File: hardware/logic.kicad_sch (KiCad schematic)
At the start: 19 parts, among them IC1 UCC2946DG4, IC2 SN74LVC1G74DCTR, IC3 SN74LVC1G74DCTR, Q1 BSS123, U1 74157, U2 4011, U3 4081, U4 4071

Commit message: kończymy balet na dziś
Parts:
- C1, C2, C3, C4: footprint Capacitor_SMD:C_0201_0603Metric_Pad0.64x0.40mm_HandSolder -> Capacitor_SMD:C_0603_1608Metric_Pad1.08x0.95mm_HandSolder
- R3, R6, R7, R8, R9: footprint Resistor_SMD:R_0603_1608Metric -> Resistor_SMD:R_0603_1608Metric_Pad0.98x0.95mm_HandSolder
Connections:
- net AS_COMMADNS+WD_OK renamed AS_COMMADNS_OK
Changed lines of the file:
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@@
     (effects (font (size 1.27 1.27)) (justify left bottom))
   )
-  (label "AS_COMMADNS+WD_OK" (at 219.71 77.47 0)
+  (label "AS_COMMADNS_OK" (at 219.71 77.47 0)
     (effects (font (size 1.27 1.27)) (justify left bottom))
   )
@@
     (property "Reference" "C4" (id 0) (at 80.01 86.36 90))
     (property "Value" "100nF" (id 1) (at 82.55 85.09 90))
-    (property "Footprint" "Capacitor_SMD:C_0201_0603Metric_Pad0.64x0.40mm_HandSolder" (id 2) (at 86.36 82.55 0)
+    (property "Footprint" "Capacitor_SMD:C_0603_1608Metric_Pad1.08x0.95mm_HandSolder" (id 2) (at 86.36 82.55 0)
       (effects (font (size 1.27 1.27)) hide)
     )
@@
       (effects (font (size 1.27 1.27)) (justify left))
     )
-    (property "Footprint" "Resistor_SMD:R_0603_1608Metric" (id 2) (at 41.91 133.35 0)
+    (property "Footprint" "Resistor_SMD:R_0603_1608Metric_Pad0.98x0.95mm_HandSolder" (id 2) (at 41.91 133.35 0)
       (effects (font (size 1.27 1.27)) hide)
     )
@@
       (effects (font (size 1.27 1.27)) (justify left))
     )
-    (property "Footprint" "Resistor_SMD:R_0603_1608Metric" (id 2) (at 63.5 120.65 0)
+    (property "Footprint" "Resistor_SMD:R_0603_1608Metric_Pad0.98x0.95mm_HandSolder" (id 2) (at 63.5 120.65 0)
       (effects (font (size 1.27 1.27)) hide)
     )
@@
       (effects (font (size 1.27 1.27)) (justify left))
     )
-    (property "Footprint" "Capacitor_SMD:C_0201_0603Metric_Pad0.64x0.40mm_HandSolder" (id 2) (at 72.39 129.54 0)
+    (property "Footprint" "Capacitor_SMD:C_0603_1608Metric_Pad1.08x0.95mm_HandSolder" (id 2) (at 72.39 129.54 0)
       (effects (font (size 1.27 1.27)) hide)
     )
@@
       (effects (font (size 1.27 1.27)) (justify left))
     )
-    (property "Footprint" "Resistor_SMD:R_0603_1608Metric" (id 2) (at 63.5 107.95 0)
+    (property "Footprint" "Resistor_SMD:R_0603_1608Metric_Pad0.98x0.95mm_HandSolder" (id 2) (at 63.5 107.95 0)
       (effects (font (size 1.27 1.27)) hide)
     )
@@
       (effects (font (size 1.27 1.27)) (justify left))
     )
-    (property "Footprint" "Resistor_SMD:R_0603_1608Metric" (id 2) (at 58.42 85.09 0)
+    (property "Footprint" "Resistor_SMD:R_0603_1608Metric_Pad0.98x0.95mm_HandSolder" (id 2) (at 58.42 85.09 0)
       (effects (font (size 1.27 1.27)) hide)
     )
@@
       (effects (font (size 1.27 1.27)) (justify left))
     )
-    (property "Footprint" "Resistor_SMD:R_0603_1608Metric" (id 2) (at 52.07 85.09 0)
+    (property "Footprint" "Resistor_SMD:R_0603_1608Metric_Pad0.98x0.95mm_HandSolder" (id 2) (at 52.07 85.09 0)
       (effects (font (size 1.27 1.27)) hide)
     )
@@
       (effects (font (size 1.27 1.27)) (justify left))
     )
-    (property "Footprint" "Capacitor_SMD:C_0201_0603Metric_Pad0.64x0.40mm_HandSolder" (id 2) (at 88.9 130.81 0)
+    (property "Footprint" "Capacitor_SMD:C_0603_1608Metric_Pad1.08x0.95mm_HandSolder" (id 2) (at 88.9 130.81 0)
       (effects (font (size 1.27 1.27)) hide)
     )
@@
       (effects (font (size 1.27 1.27)) (justify left))
     )
-    (property "Footprint" "Capacitor_SMD:C_0201_0603Metric_Pad0.64x0.40mm_HandSolder" (id 2) (at 82.55 109.22 0)
-      (effects (font (size 1.27 1.27)) hide)
-    )
+    (property "Footprint" "Capacitor_SMD:C_0603_1608Metric_Pad1.08x0.95mm_HandSolder" (id 2) (at 82.55 109.22 0)
+      (effects (font (size 1.27 1.27)) hide)
+    )

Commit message: kurde no jeszcze nie skonczylem ale sune dalej
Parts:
- C32, C33: footprint Capacitor_SMD:C_0201_0603Metric_Pad0.64x0.40mm_HandSolder -> Capacitor_SMD:C_0603_1608Metric_Pad1.08x0.95mm_HandSolder
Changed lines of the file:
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@@
       (effects (font (size 1.27 1.27)) (justify left))
     )
-    (property "Footprint" "Capacitor_SMD:C_0201_0603Metric_Pad0.64x0.40mm_HandSolder" (id 2) (at 205.74 31.75 0)
+    (property "Footprint" "Capacitor_SMD:C_0603_1608Metric_Pad1.08x0.95mm_HandSolder" (id 2) (at 205.74 31.75 0)
       (effects (font (size 1.27 1.27)) hide)
     )
@@
       (effects (font (size 1.27 1.27)) (justify left))
     )
-    (property "Footprint" "Capacitor_SMD:C_0201_0603Metric_Pad0.64x0.40mm_HandSolder" (id 2) (at 237.49 38.1 0)
+    (property "Footprint" "Capacitor_SMD:C_0603_1608Metric_Pad1.08x0.95mm_HandSolder" (id 2) (at 237.49 38.1 0)
       (effects (font (size 1.27 1.27)) hide)
     )

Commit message: fixed references addet tp;s mam pojutrze przejebany egzamin nara
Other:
- note added: "AND2"
- note added: "NAND1"
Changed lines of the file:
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@@
     (effects (font (size 1.27 1.27) italic) (justify left bottom))
+  )
+  (text "AND2" (at 149.86 146.05 0)
+    (effects (font (size 1.27 1.27)) (justify left bottom))
+  )
+  (text "NAND1" (at 147.32 71.12 0)
+    (effects (font (size 1.27 1.27)) (justify left bottom))
   )
   (text "WD operation:\nPage 7 of Datasheet" (at 99.06 102.87 0)

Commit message: L4 port
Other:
- note added: "07072023 zwora do ominięcia przycisków"

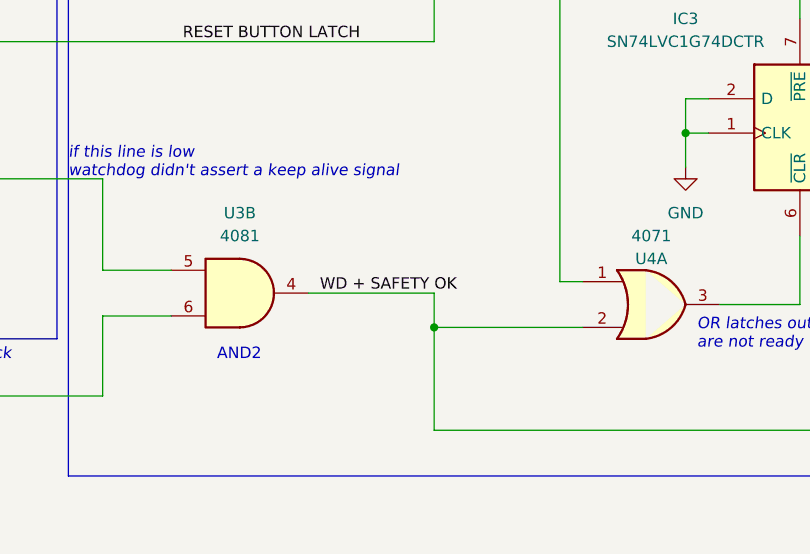
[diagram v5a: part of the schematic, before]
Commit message: first working state, valves forced activation
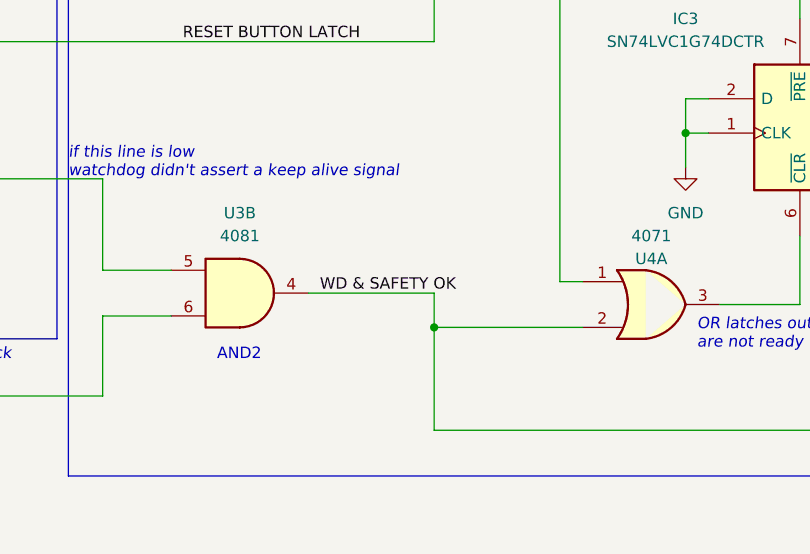
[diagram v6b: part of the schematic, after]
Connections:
- net WD + SAFETY OK renamed WD & SAFETY OK
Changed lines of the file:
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@@
     (effects (font (size 1.27 1.27)) (justify left bottom))
   )
-  (label "WD + SAFETY OK" (at 161.29 138.43 0) (fields_autoplaced)
+  (label "WD & SAFETY OK" (at 161.29 138.43 0) (fields_autoplaced)
     (effects (font (size 1.27 1.27)) (justify left bottom))
   )

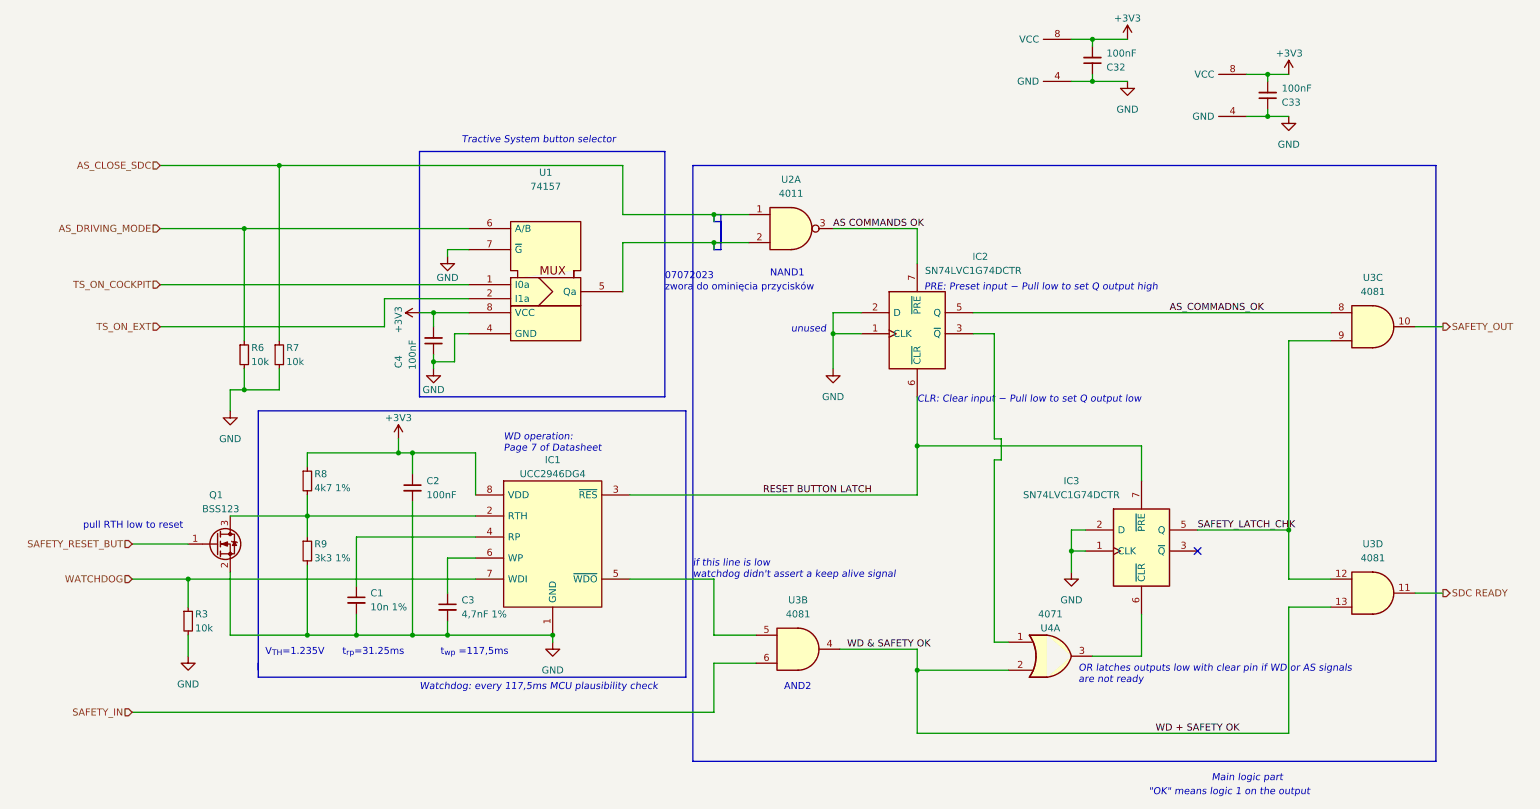
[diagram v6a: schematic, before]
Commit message: Schematic redesign for 23 rules, new pressure buffer, protection fix
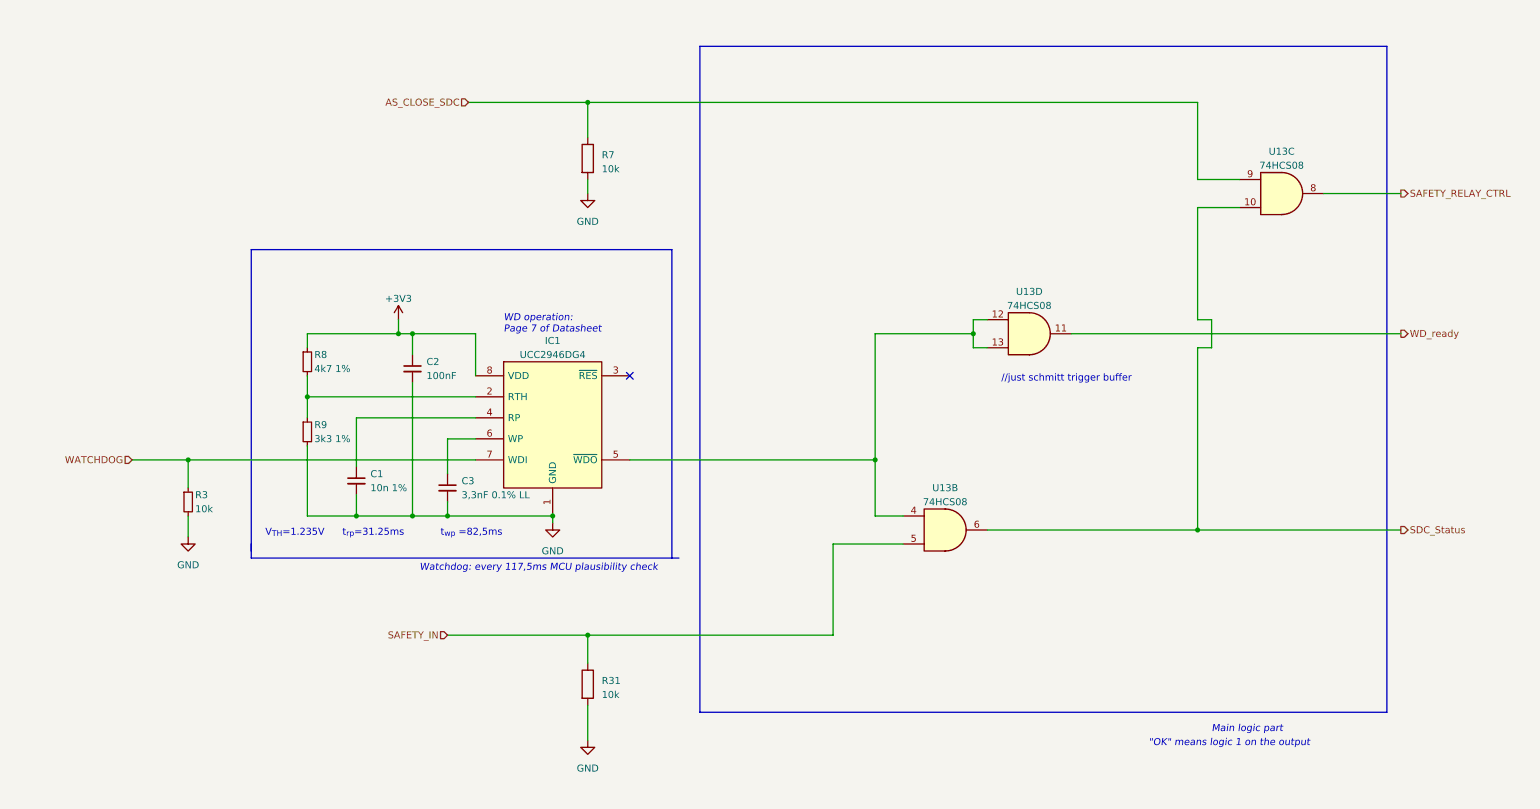
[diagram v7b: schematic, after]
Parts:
- removed C32, C33, C4: 100nF, Capacitor_SMD:C_0603_1608Metric_Pad1.08x0.95mm_HandSolder, symbol Device:C_Small
- removed IC2, IC3: SN74LVC1G74DCTR, SamacSys_Parts:SOP65P400X130-8N, symbol SamacSys_Parts:SN74LVC1G74DCTR
- removed Q1: BSS123, Package_TO_SOT_SMD:SOT-23, symbol Transistor_FET:BSS123
- removed R6, R7: 10k, Resistor_SMD:R_0603_1608Metric_Pad0.98x0.95mm_HandSolder, symbol Device:R_Small
- removed U1: 74157, Package_SO:VSSOP-8_2.3x2mm_P0.5mm, symbol 74xx_IEEE:74157
- removed U2: 4011, Package_SO:TSSOP-14_4.4x5mm_P0.65mm, symbol 4xxx:4011
- removed U3: 4081, Package_SO:TSSOP-14_4.4x5mm_P0.65mm, symbol 4xxx:4081
- removed U4: 4071, Package_SO:TSSOP-14_4.4x5mm_P0.65mm, symbol 4xxx:4071
- added R31, R7: 10k, Resistor_SMD:R_0603_1608Metric_Pad0.98x0.95mm_HandSolder, symbol Device:R
- added U13: 74HCS08, Package_SO:SOIC-14_3.9x8.7mm_P1.27mm, symbol 74xx:74LS08
- C3: value 4,7nF 1% -> 3,3nF 0.1% LL
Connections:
- net AS_CLOSE_SDC: now also R7.1, U13.9
- net GND: now also R31.2, R7.2
- net SAFETY_IN: now also R31.1, U13.5
- net at IC1.5 (~{WDO}): now also U13.12, U13.13, U13.4
- net RESET BUTTON LATCH: no longer names the net of IC1.3 (~{RES})
- new net SAFETY_RELAY_CTRL: U13.8
- new net SDC_Status: U13.10, U13.6
- new net WD_ready: U13.11
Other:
- note added: "//just schmitt trigger buffer"
- note added: "t_{wp} =82,5ms"
- note removed: "07072023 zwora do ominięcia przycisków"
- note removed: "AND2"
- note removed: "CLR: Clear input − Pull low to set Q output low"
- note removed: "NAND1"
- note removed: "OR latches outputs low with clear pin if WD or AS signals are not ready"
- note removed: "PRE: Preset input − Pull low to set Q output high"
- note removed: "Tractive System button selector"
- note removed: "if this line is low watchdog didn't assert a keep alive signal"
- note removed: "pull RTH low to reset"
- note removed: "t_{wp} =117,5ms"
- note removed: "unused"
- moved on the sheet: C1, C2, C3, IC1, R3, R8, R9

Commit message: WIP revision 2 layout refinement
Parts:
- removed U13: 74HCS08, Package_SO:SOIC-14_3.9x8.7mm_P1.27mm, symbol 74xx:74LS08
- added C23, C27, C4: 100nF, Capacitor_SMD:C_0603_1608Metric_Pad1.08x0.95mm_HandSolder, symbol Device:C_Small
- added U10, U8, U9: 74LVC1G08, Package_TO_SOT_SMD:SOT-353_SC-70-5_Handsoldering, symbol 74xGxx:74LVC1G08
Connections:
- net +3V3: now also C23.2, C27.2, C4.2, U10.5 (VCC), U8.5 (VCC), U9.5 (VCC)
- net AS_CLOSE_SDC: now also U10.1
- net GND: now also C23.1, C27.1, C4.1, U10.3 (GND), U8.3 (GND), U9.3 (GND)
- net SAFETY_IN: now also U8.2
- net SAFETY_RELAY_CTRL: now also U10.4
- net SDC_Status: now also U10.2, U8.4
- net WD_ready: now also U9.4
- net at IC1.5 (~{WDO}): now also U8.1, U9.1, U9.2
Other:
- note added: "NEXPERIA ones w/ schmitt trigger"
